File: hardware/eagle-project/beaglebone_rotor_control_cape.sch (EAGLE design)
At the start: 57 parts, among them IC1 TLC2264CDU, IC2 MCP4901, IC3 MAX3232ESE, IC4 TLC2264CDU, IC5 MCP4901, IC6 TLC2264CDU, Q1 SQ2348ES-T1-GE3, Q2 SQ2348ES-T1-GE3, Q3 SQ2348ES-T1-GE3, Q4 SQ2348ES-T1-GE3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

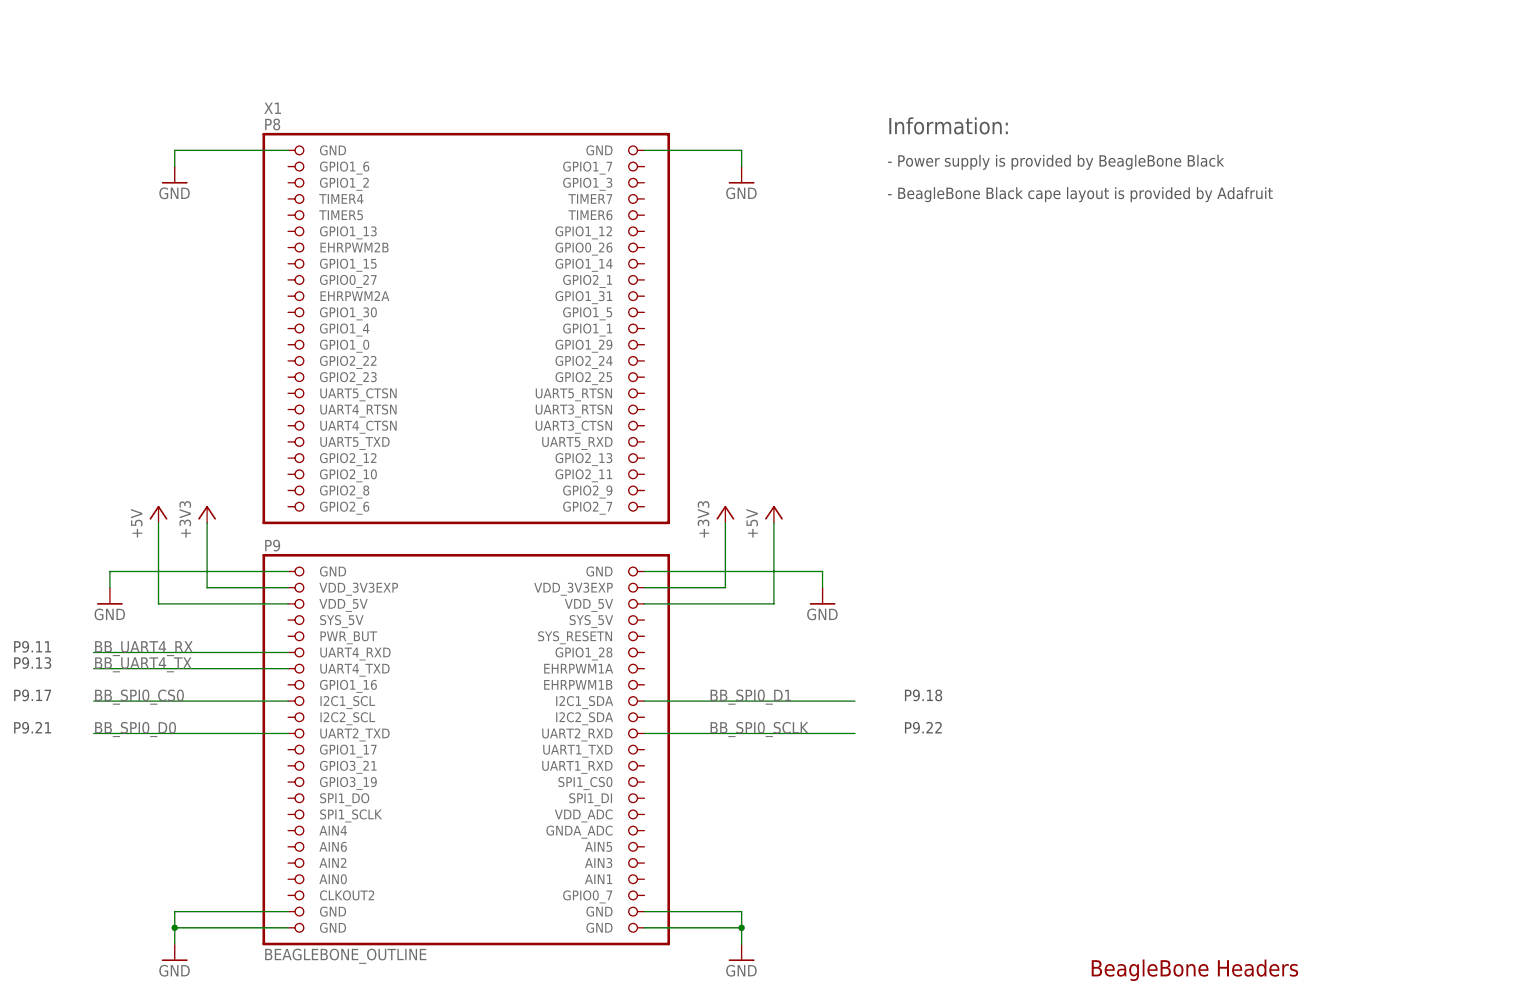
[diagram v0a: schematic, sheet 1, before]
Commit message: * layout: added spi1 and determined pin for usb slave turn on
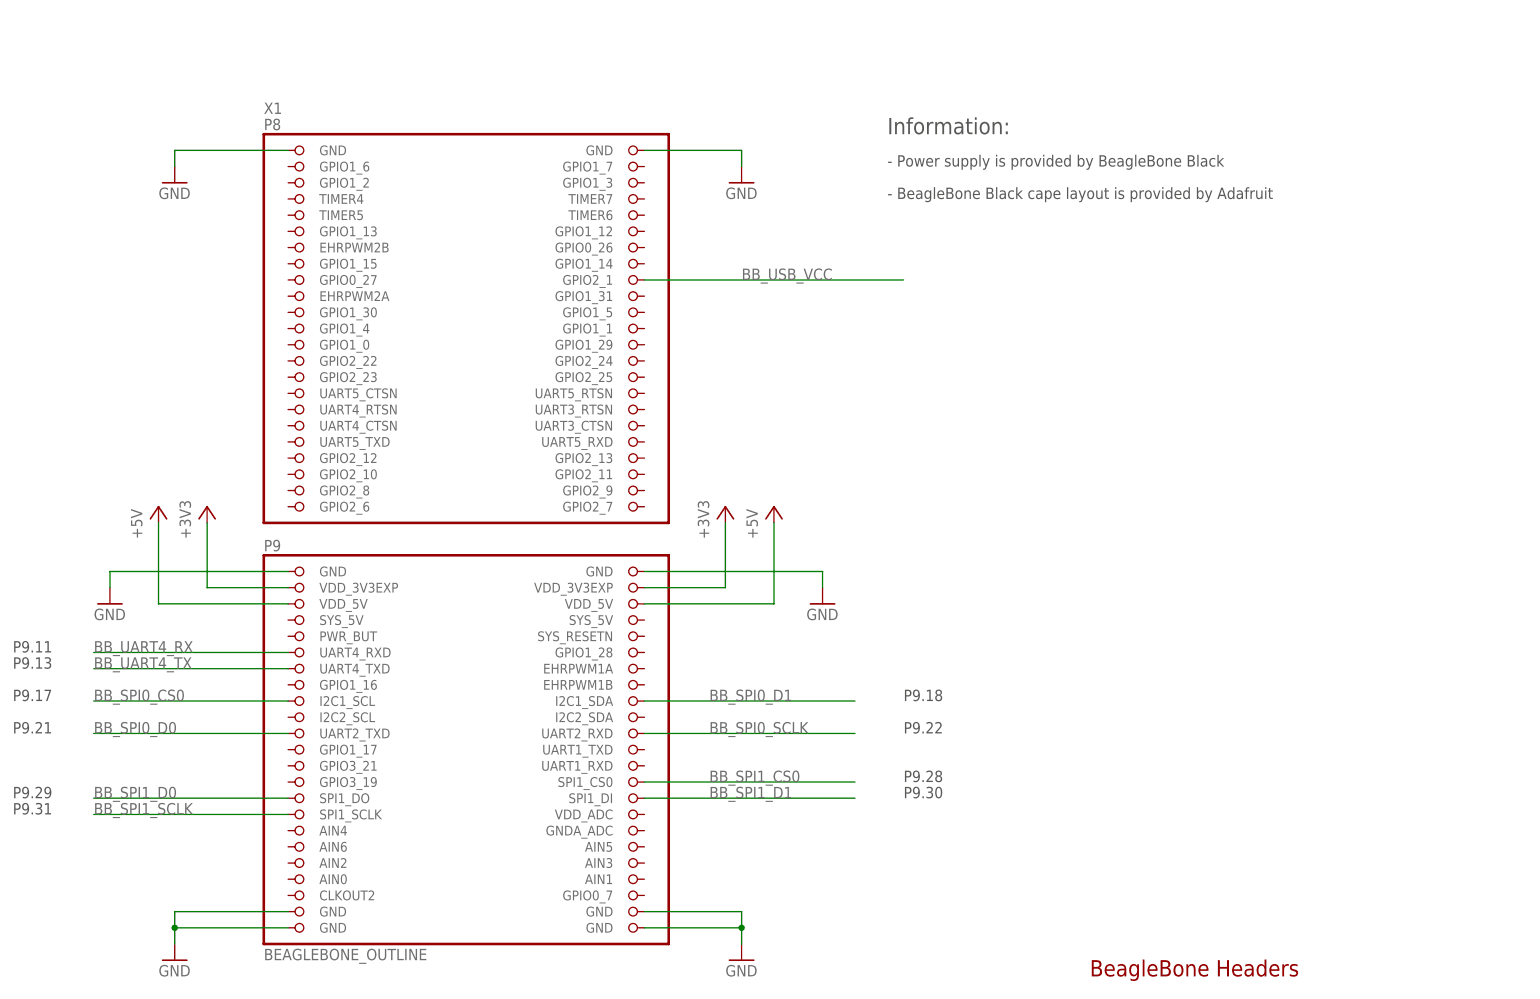
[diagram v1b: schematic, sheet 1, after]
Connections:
- removed net N$23: R25.1
- removed net N$24: R24.1
- removed net N$26: R23.1
- new net BB_SPI1_CS0: R25.1, X1.SPI1_CS0
- new net BB_SPI1_D0: R23.1, X1.SPI1_DO
- new net BB_SPI1_D1: X1.SPI1_DI
- new net BB_SPI1_SCLK: R24.1, X1.SPI1_SCLK
- new net BB_USB_VCC: X1.GPIO2_1
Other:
- note added: "P9.28"
- note added: "P9.29"
- note added: "P9.30"
- note added: "P9.31"
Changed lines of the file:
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@@
 <text x="10.16" y="68.58" size="1.778" layer="97">P9.13</text>
 <text x="10.16" y="71.12" size="1.778" layer="97">P9.11</text>
+<text x="10.16" y="48.26" size="1.778" layer="97">P9.29</text>
+<text x="149.86" y="48.26" size="1.778" layer="97">P9.30</text>
+<text x="10.16" y="45.72" size="1.778" layer="97">P9.31</text>
+<text x="149.86" y="50.8" size="1.778" layer="97">P9.28</text>
 </plain>
 <instances>
@@
 <wire x1="109.22" y1="58.42" x2="142.24" y2="58.42" width="0.1524" layer="91"/>
 <label x="119.38" y="58.42" size="1.778" layer="95"/>
+</segment>
+</net>
+<net name="BB_USB_VCC" class="0">
+<segment>
+<pinref part="X1" gate="G$1" pin="GPIO2_1"/>
+<wire x1="109.22" y1="129.54" x2="149.86" y2="129.54" width="0.1524" layer="91"/>
+<label x="124.46" y="129.54" size="1.778" layer="95"/>
+</segment>
+</net>
+<net name="BB_SPI1_CS0" class="0">
+<segment>
+<pinref part="X1" gate="G$1" pin="SPI1_CS0"/>
+<wire x1="109.22" y1="50.8" x2="142.24" y2="50.8" width="0.1524" layer="91"/>
+<label x="119.38" y="50.8" size="1.778" layer="95"/>
+</segment>
+</net>
+<net name="BB_SPI1_SCLK" class="0">
+<segment>
+<pinref part="X1" gate="G$1" pin="SPI1_SCLK"/>
+<wire x1="53.34" y1="45.72" x2="22.86" y2="45.72" width="0.1524" layer="91"/>
+<label x="22.86" y="45.72" size="1.778" layer="95"/>
+</segment>
+</net>
+<net name="BB_SPI1_D1" class="0">
+<segment>
+<pinref part="X1" gate="G$1" pin="SPI1_DI"/>
+<wire x1="109.22" y1="48.26" x2="142.24" y2="48.26" width="0.1524" layer="91"/>
+<label x="119.38" y="48.26" size="1.778" layer="95"/>
+</segment>
+</net>
+<net name="BB_SPI1_D0" class="0">
+<segment>
+<pinref part="X1" gate="G$1" pin="SPI1_DO"/>
+<wire x1="53.34" y1="48.26" x2="22.86" y2="48.26" width="0.1524" layer="91"/>
+<label x="22.86" y="48.26" size="1.778" layer="95"/>
 </segment>
 </net>
@@
 </segment>
 </net>
-<net name="N$23" class="0">
+<net name="BB_SPI1_CS0" class="0">
 <segment>
 <pinref part="R25" gate="G$1" pin="1"/>
@@
 </segment>
 </net>
-<net name="N$24" class="0">
+<net name="BB_SPI1_SCLK" class="0">
 <segment>
 <pinref part="R24" gate="G$1" pin="1"/>
@@
 </segment>
 </net>
-<net name="N$26" class="0">
+<net name="BB_SPI1_D0" class="0">
 <segment>
 <pinref part="R23" gate="G$1" pin="1"/>

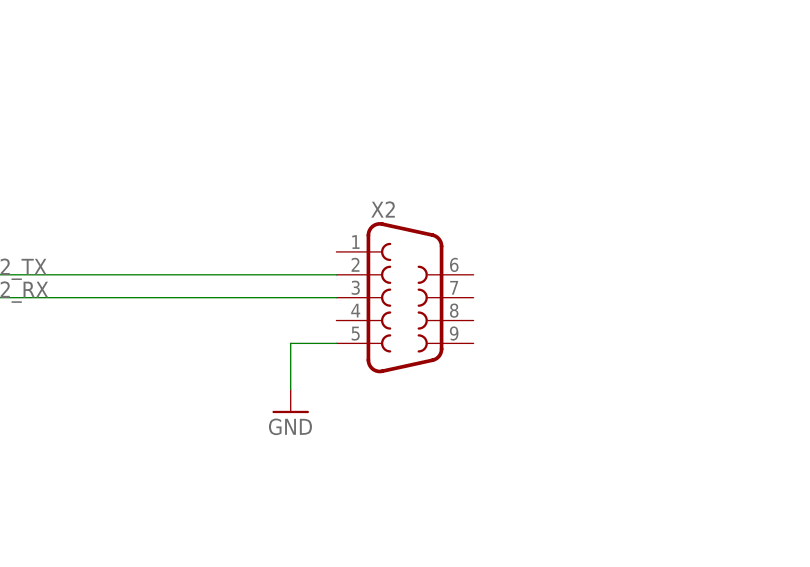
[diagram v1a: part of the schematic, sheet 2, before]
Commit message: Created library for D-Sub connector from TE.com
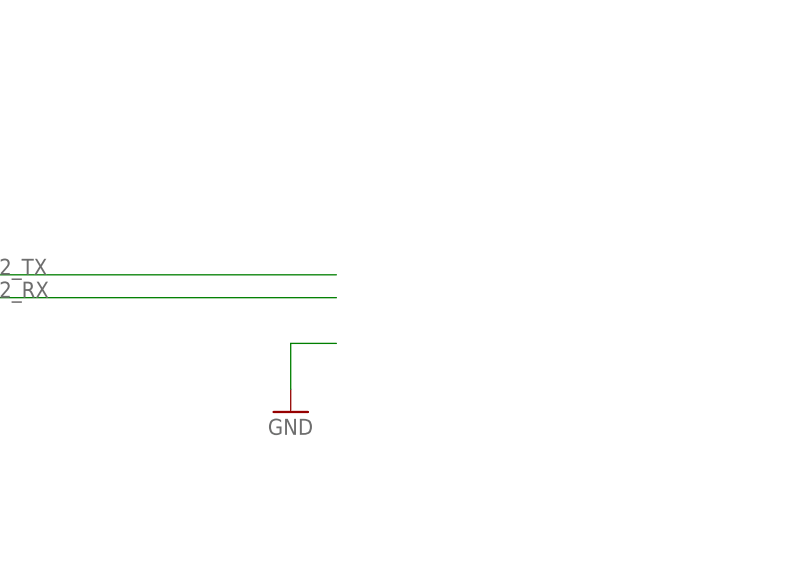
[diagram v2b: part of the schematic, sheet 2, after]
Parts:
- removed X2: (no value), con-subd:F09VP
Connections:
- net GND: no longer X2.5
- net RS232_RX: no longer X2.3
- net RS232_TX: no longer X2.2
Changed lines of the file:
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@@
 <part name="R8" library="rcl" deviceset="R-EU_" device="R0805" value="100"/>
 <part name="R1" library="rcl" deviceset="R-EU_" device="R0805" value="100"/>
-<part name="X2" library="con-subd" deviceset="F09" device="VP"/>
 <part name="FRAME4" library="frames_2" deviceset="A4L-LOC" device=""/>
 <part name="R10" library="rcl" deviceset="R-EU_" device="R0805" value="10k"/>
@@
 <instance part="R8" gate="G$1" x="134.62" y="119.38"/>
 <instance part="R1" gate="G$1" x="142.24" y="114.3"/>
-<instance part="X2" gate="G$1" x="93.98" y="60.96"/>
 <instance part="IC3" gate="P" x="43.18" y="127"/>
 <instance part="+3V3" gate="G$1" x="43.18" y="142.24"/>
@@
 </segment>
 <segment>
-<pinref part="X2" gate="G$1" pin="5"/>
 <wire x1="86.36" y1="55.88" x2="81.28" y2="55.88" width="0.1524" layer="91"/>
 <wire x1="81.28" y1="55.88" x2="81.28" y2="50.8" width="0.1524" layer="91"/>
@@
 </segment>
 <segment>
-<pinref part="X2" gate="G$1" pin="2"/>
 <wire x1="86.36" y1="63.5" x2="43.18" y2="63.5" width="0.1524" layer="91"/>
 <label x="43.18" y="63.5" size="1.778" layer="95"/>
@@
 </segment>
 <segment>
-<pinref part="X2" gate="G$1" pin="3"/>
 <wire x1="86.36" y1="60.96" x2="43.18" y2="60.96" width="0.1524" layer="91"/>
 <label x="43.18" y="60.96" size="1.778" layer="95"/>

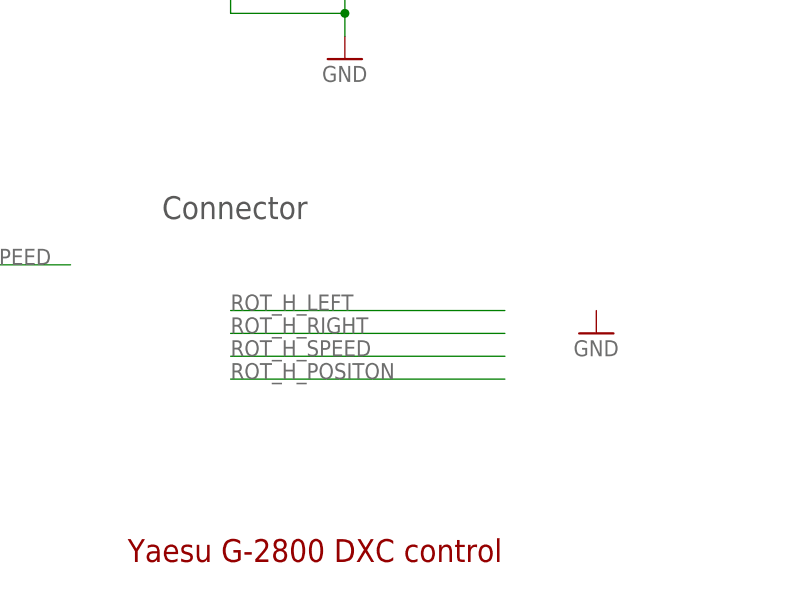
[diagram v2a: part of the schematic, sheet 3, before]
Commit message: Placed D-Sub connectors on layout
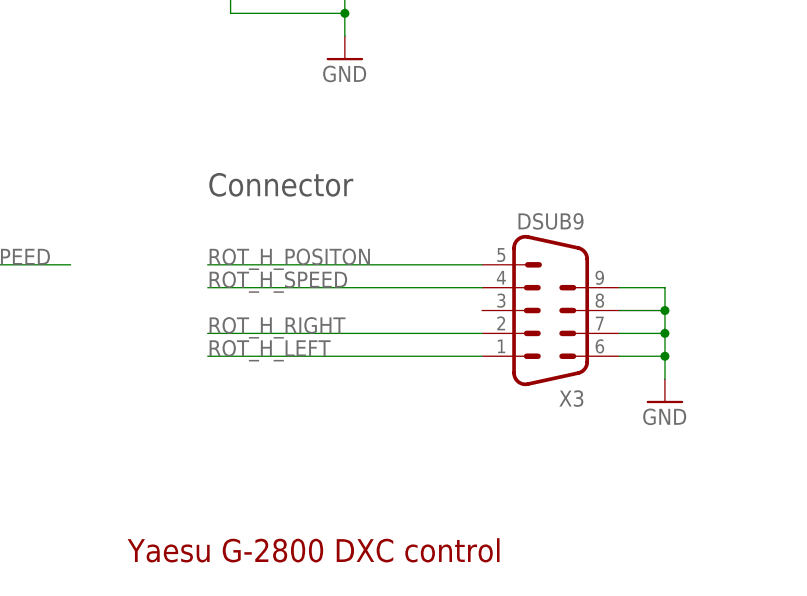
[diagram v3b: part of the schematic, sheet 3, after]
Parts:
- added X2, X3, X4: DSUB9, con-te-dsub:DSUB9
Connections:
- net GND: now also X3.6, X3.7, X3.8, X3.9, X4.6, X4.7, X4.8, X4.9
- net ROT_E_DOWN: now also X4.2
- net ROT_E_POSITION: now also X4.5
- net ROT_E_SPEED: now also X4.4
- net ROT_E_UP: now also X4.1
- net ROT_H_LEFT: now also X3.1
- net ROT_H_POSITON: now also X3.5
- net ROT_H_RIGHT: now also X3.2
- net ROT_H_SPEED: now also X3.4
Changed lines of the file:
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@@
 <part name="R31" library="rcl" deviceset="R-EU_" device="R0805" value="100"/>
 <part name="R32" library="rcl" deviceset="R-EU_" device="R0805" value="100"/>
+<part name="X2" library="con-te-dsub" deviceset="DSUB9" device=""/>
+<part name="X3" library="con-te-dsub" deviceset="DSUB9" device=""/>
+<part name="X4" library="con-te-dsub" deviceset="DSUB9" device=""/>
+<part name="GND31" library="supply1" deviceset="GND" device=""/>
 </parts>
 <sheets>
@@
 <instance part="C6" gate="G$1" x="55.88" y="129.54"/>
 <instance part="GND16" gate="1" x="81.28" y="48.26"/>
+<instance part="X2" gate="G$1" x="99.06" y="58.42"/>
 </instances>
 <busses>
@@
 <text x="15.24" y="157.48" size="5.08" layer="97">Yaesu G-2800 DXC</text>
 <text x="15.24" y="93.98" size="2.54" layer="97">Speed output (analog, 0.5 - 4.5V)</text>
-<text x="182.88" y="58.42" size="2.54" layer="97">Connector</text>
+<text x="187.96" y="60.96" size="2.54" layer="97">Connector</text>
 <text x="106.68" y="124.46" size="1.778" layer="97" rot="R90">lieber Uz=4.7V?, aber
 Signal geht bis 5V (???)
@@
 <instance part="C7" gate="G$1" x="99.06" y="78.74"/>
 <instance part="GND17" gate="1" x="99.06" y="68.58"/>
-<instance part="GND18" gate="1" x="231.14" y="45.72"/>
+<instance part="GND18" gate="1" x="238.76" y="38.1"/>
 <instance part="IC2" gate="G$1" x="76.2" y="55.88"/>
 <instance part="R11" gate="G$1" x="48.26" y="38.1" rot="R90"/>
@@
 <instance part="R20" gate="G$1" x="48.26" y="55.88"/>
 <instance part="R21" gate="G$1" x="38.1" y="45.72"/>
+<instance part="X3" gate="G$1" x="226.06" y="48.26" rot="R180"/>
 </instances>
 <busses>
@@
 <wire x1="134.62" y1="22.86" x2="134.62" y2="25.4" width="0.1524" layer="91"/>
 </segment>
+<segment>
+<pinref part="X3" gate="G$1" pin="6"/>
+<pinref part="GND18" gate="1" pin="GND"/>
+<wire x1="233.68" y1="43.18" x2="238.76" y2="43.18" width="0.1524" layer="91"/>
+<wire x1="238.76" y1="43.18" x2="238.76" y2="40.64" width="0.1524" layer="91"/>
+<pinref part="X3" gate="G$1" pin="7"/>
+<wire x1="233.68" y1="45.72" x2="238.76" y2="45.72" width="0.1524" layer="91"/>
+<wire x1="238.76" y1="45.72" x2="238.76" y2="43.18" width="0.1524" layer="91"/>
+<junction x="238.76" y="43.18"/>
+<pinref part="X3" gate="G$1" pin="8"/>
+<wire x1="233.68" y1="48.26" x2="238.76" y2="48.26" width="0.1524" layer="91"/>
+<wire x1="238.76" y1="48.26" x2="238.76" y2="45.72" width="0.1524" layer="91"/>
+<junction x="238.76" y="45.72"/>
+<pinref part="X3" gate="G$1" pin="9"/>
+<wire x1="233.68" y1="50.8" x2="238.76" y2="50.8" width="0.1524" layer="91"/>
+<wire x1="238.76" y1="50.8" x2="238.76" y2="48.26" width="0.1524" layer="91"/>
+<junction x="238.76" y="48.26"/>
+</segment>
 </net>
 <net name="ROT_H_LEFT" class="0">
@@
 </segment>
 <segment>
-<wire x1="190.5" y1="48.26" x2="220.98" y2="48.26" width="0.1524" layer="91"/>
-<label x="190.5" y="48.26" size="1.778" layer="95"/>
+<wire x1="187.96" y1="43.18" x2="218.44" y2="43.18" width="0.1524" layer="91"/>
+<label x="187.96" y="43.18" size="1.778" layer="95"/>
+<pinref part="X3" gate="G$1" pin="1"/>
 </segment>
 </net>
@@
 </segment>
 <segment>
-<wire x1="220.98" y1="45.72" x2="190.5" y2="45.72" width="0.1524" layer="91"/>
-<label x="190.5" y="45.72" size="1.778" layer="95"/>
+<wire x1="218.44" y1="45.72" x2="187.96" y2="45.72" width="0.1524" layer="91"/>
+<label x="187.96" y="45.72" size="1.778" layer="95"/>
+<pinref part="X3" gate="G$1" pin="2"/>
 </segment>
 </net>
@@
 </segment>
 <segment>
-<wire x1="220.98" y1="40.64" x2="190.5" y2="40.64" width="0.1524" layer="91"/>
-<label x="190.5" y="40.64" size="1.778" layer="95"/>
+<wire x1="218.44" y1="53.34" x2="187.96" y2="53.34" width="0.1524" layer="91"/>
+<label x="187.96" y="53.34" size="1.778" layer="95"/>
+<pinref part="X3" gate="G$1" pin="5"/>
 </segment>
 </net>
@@
 </segment>
 <segment>
-<wire x1="190.5" y1="43.18" x2="220.98" y2="43.18" width="0.1524" layer="91"/>
-<label x="190.5" y="43.18" size="1.778" layer="95"/>
+<wire x1="187.96" y1="50.8" x2="218.44" y2="50.8" width="0.1524" layer="91"/>
+<label x="187.96" y="50.8" size="1.778" layer="95"/>
+<pinref part="X3" gate="G$1" pin="4"/>
 </segment>
 </net>
@@
 <instance part="R31" gate="G$1" x="177.8" y="91.44"/>
 <instance part="R32" gate="G$1" x="175.26" y="142.24"/>
+<instance part="X4" gate="G$1" x="233.68" y="45.72" rot="R180"/>
+<instance part="GND31" gate="1" x="246.38" y="33.02"/>
 </instances>
 <busses>
@@
 <wire x1="203.2" y1="76.2" x2="203.2" y2="88.9" width="0.1524" layer="91"/>
 <junction x="203.2" y="76.2"/>
+</segment>
+<segment>
+<pinref part="GND31" gate="1" pin="GND"/>
+<pinref part="X4" gate="G$1" pin="6"/>
+<pinref part="X4" gate="G$1" pin="7"/>
+<wire x1="241.3" y1="43.18" x2="246.38" y2="43.18" width="0.1524" layer="91"/>
+<wire x1="246.38" y1="43.18" x2="246.38" y2="40.64" width="0.1524" layer="91"/>
+<pinref part="X4" gate="G$1" pin="8"/>
+<wire x1="246.38" y1="40.64" x2="246.38" y2="35.56" width="0.1524" layer="91"/>
+<wire x1="241.3" y1="45.72" x2="246.38" y2="45.72" width="0.1524" layer="91"/>
+<wire x1="246.38" y1="45.72" x2="246.38" y2="43.18" width="0.1524" layer="91"/>
+<junction x="246.38" y="43.18"/>
+<wire x1="241.3" y1="40.64" x2="246.38" y2="40.64" width="0.1524" layer="91"/>
+<junction x="246.38" y="40.64"/>
+<pinref part="X4" gate="G$1" pin="9"/>
+<wire x1="241.3" y1="48.26" x2="246.38" y2="48.26" width="0.1524" layer="91"/>
+<wire x1="246.38" y1="48.26" x2="246.38" y2="45.72" width="0.1524" layer="91"/>
+<junction x="246.38" y="45.72"/>
 </segment>
 </net>
@@
 <wire x1="144.78" y1="48.26" x2="170.18" y2="48.26" width="0.1524" layer="91"/>
 <label x="149.86" y="48.26" size="1.778" layer="95"/>
+</segment>
+<segment>
+<pinref part="X4" gate="G$1" pin="4"/>
+<wire x1="195.58" y1="48.26" x2="226.06" y2="48.26" width="0.1524" layer="91"/>
+<label x="195.58" y="48.26" size="1.778" layer="95"/>
 </segment>
 </net>
@@
 <label x="121.92" y="124.46" size="1.778" layer="95"/>
 </segment>
+<segment>
+<pinref part="X4" gate="G$1" pin="5"/>
+<wire x1="226.06" y1="50.8" x2="195.58" y2="50.8" width="0.1524" layer="91"/>
+<label x="195.58" y="50.8" size="1.778" layer="95"/>
+</segment>
 </net>
 <net name="N$34" class="0">
@@
 <label x="213.36" y="101.6" size="1.778" layer="95"/>
 </segment>
+<segment>
+<pinref part="X4" gate="G$1" pin="2"/>
+<wire x1="226.06" y1="43.18" x2="195.58" y2="43.18" width="0.1524" layer="91"/>
+<label x="195.58" y="43.18" size="1.778" layer="95"/>
+</segment>
 </net>
 <net name="ROT_E_UP" class="0">
@@
 <label x="213.36" y="152.4" size="1.778" layer="95"/>
 </segment>
-</net>
+<segment>
+<pinref part="X4" gate="G$1" pin="1"/>
+<wire x1="195.58" y1="40.64" x2="226.06" y2="40.64" width="0.1524" layer="91"/>
+<label x="195.58" y="40.64" size="1.778" layer="95"/>
+</segment>
+</net>
